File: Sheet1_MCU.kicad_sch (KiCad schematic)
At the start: 16 parts, among them U1 nRF52840-QIAA, Y1 32MHz, Y2 32.77kHz

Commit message: Fix: Applied footprint corrections and added missing libraries to tables
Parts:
- ANT1: footprint Capacitor_SMD:C_0402_1005Metric -> RF_Antenna:Johanson_2450AT18x100
- U1: footprint (none) -> Package_DFN_QFN:Nordic_AQFN-73-1EP_7x7mm_P0.5mm
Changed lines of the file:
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@@
 			)
 		)
-		(property "Footprint" "Capacitor_SMD:C_0402_1005Metric"
+		(property "Footprint" "RF_Antenna:Johanson_2450AT18x100"
 			(at 185 250 0)
 			(effects
@@
 			)
 		)
-		(property "Footprint" ""
+		(property "Footprint" "Package_DFN_QFN:Nordic_AQFN-73-1EP_7x7mm_P0.5mm"
 			(at 200 150 0)
 			(effects

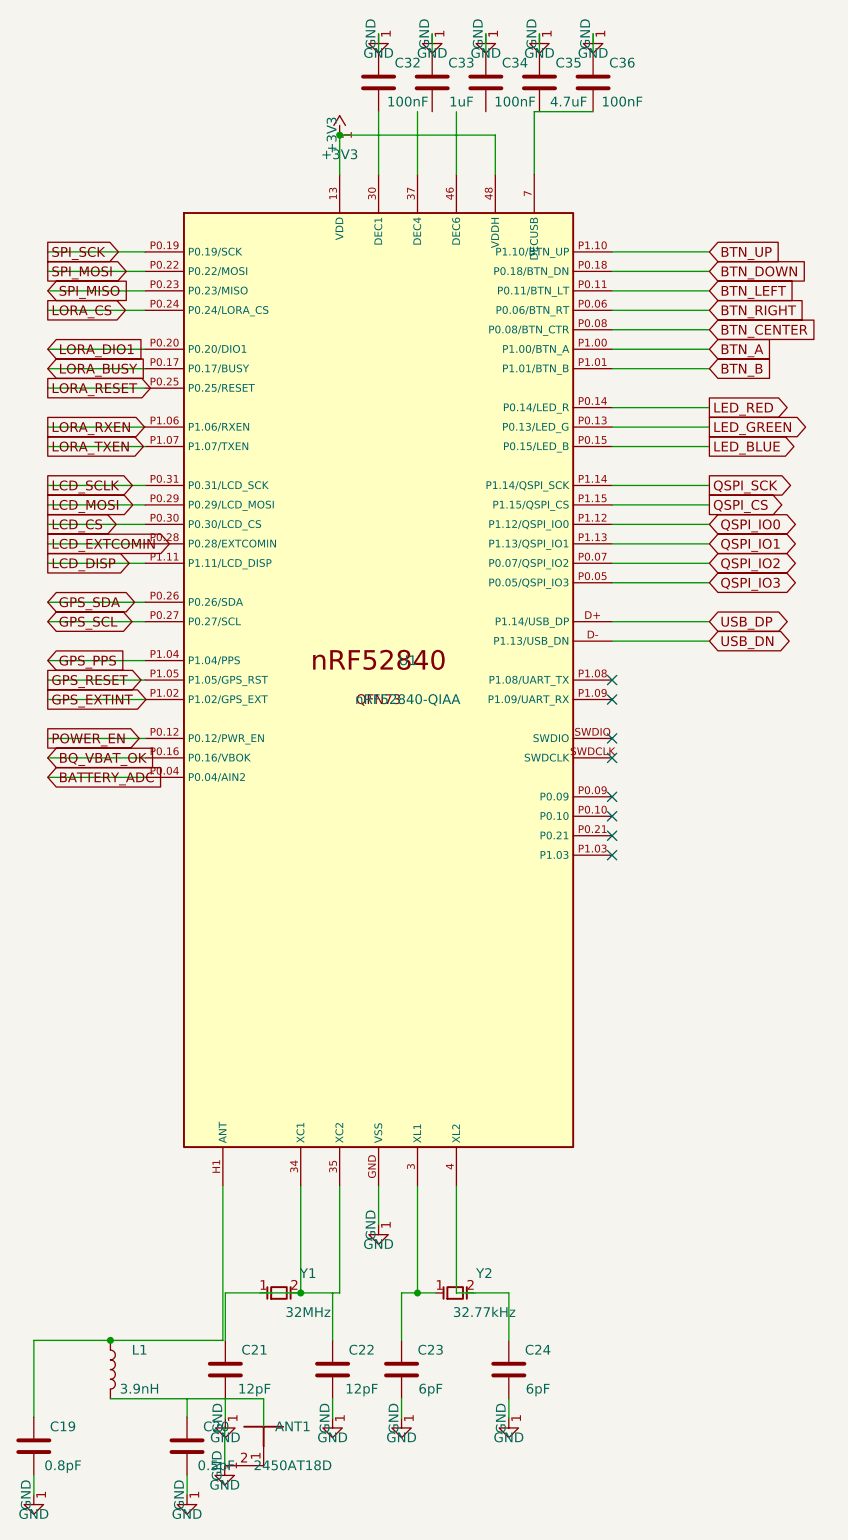
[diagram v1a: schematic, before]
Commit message: Fix: Comprehensive error resolution (nRF52840 pin remapping, footprint rebuilding)
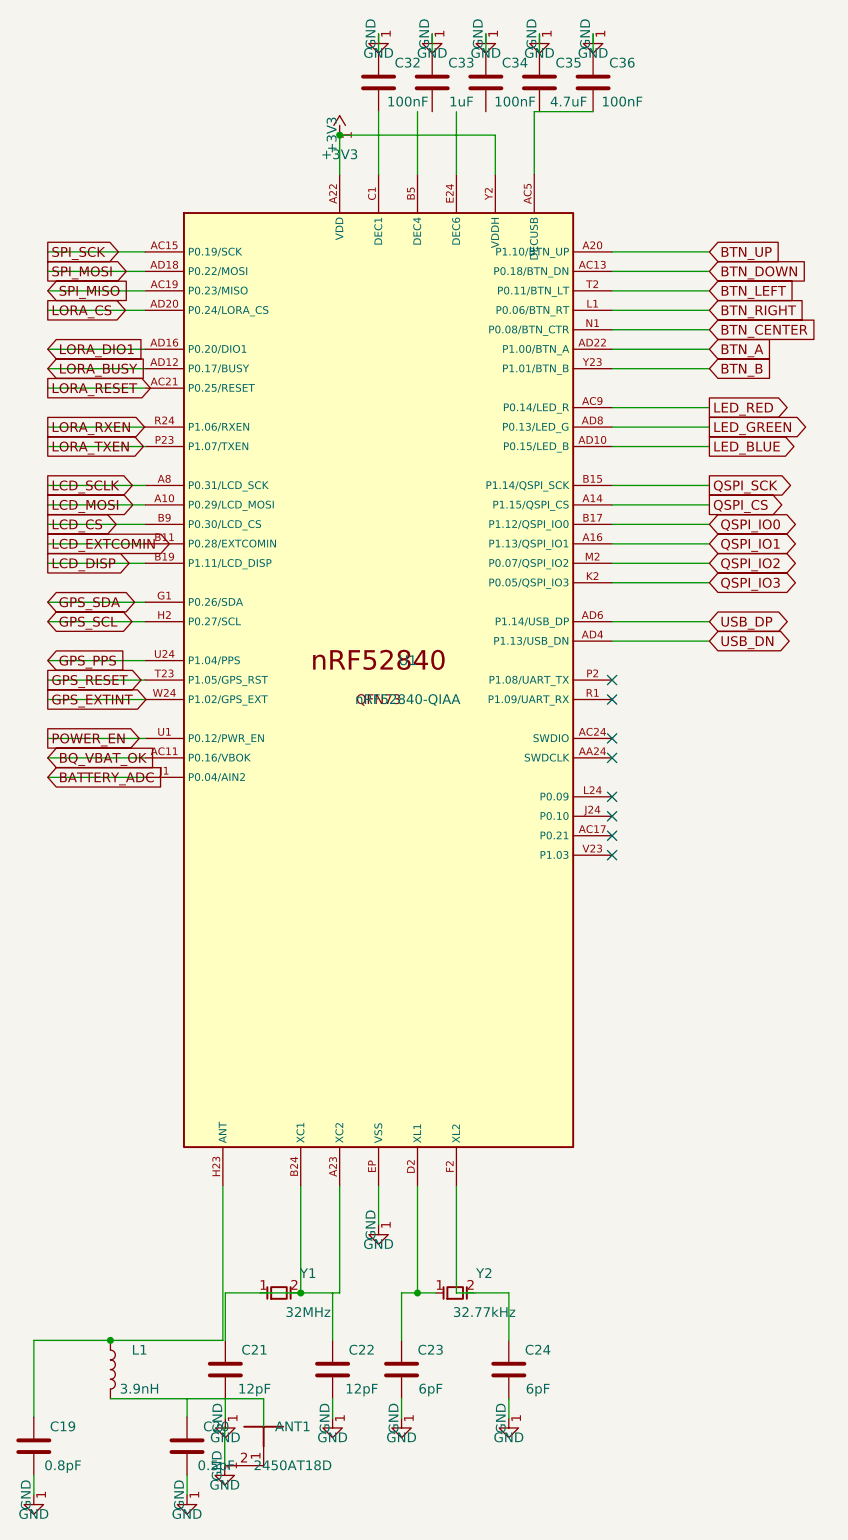
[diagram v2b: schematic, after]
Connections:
- net +3V3: now also U1.A22 (VDD), U1.Y2 (VDDH); no longer U1.13 (VDD), U1.48 (VDDH)
- net BATTERY_ADC: now also U1.J1 (P0.04/AIN2); no longer U1.P0.04 (P0.04/AIN2)
- net BQ_VBAT_OK: now also U1.AC11 (P0.16/VBOK); no longer U1.P0.16 (P0.16/VBOK)
- net BTN_A: now also U1.AD22 (P1.00/BTN_A); no longer U1.P1.00 (P1.00/BTN_A)
- net BTN_B: now also U1.Y23 (P1.01/BTN_B); no longer U1.P1.01 (P1.01/BTN_B)
- net BTN_CENTER: now also U1.N1 (P0.08/BTN_CTR); no longer U1.P0.08 (P0.08/BTN_CTR)
- net BTN_DOWN: now also U1.AC13 (P0.18/BTN_DN); no longer U1.P0.18 (P0.18/BTN_DN)
- net BTN_LEFT: now also U1.T2 (P0.11/BTN_LT); no longer U1.P0.11 (P0.11/BTN_LT)
- net BTN_RIGHT: now also U1.L1 (P0.06/BTN_RT); no longer U1.P0.06 (P0.06/BTN_RT)
- net BTN_UP: now also U1.A20 (P1.10/BTN_UP); no longer U1.P1.10 (P1.10/BTN_UP)
- net GND: now also U1.EP (VSS); no longer U1.GND (VSS)
- net GPS_EXTINT: now also U1.W24 (P1.02/GPS_EXT); no longer U1.P1.02 (P1.02/GPS_EXT)
- net GPS_PPS: now also U1.U24 (P1.04/PPS); no longer U1.P1.04 (P1.04/PPS)
- net GPS_RESET: now also U1.T23 (P1.05/GPS_RST); no longer U1.P1.05 (P1.05/GPS_RST)
- net GPS_SCL: now also U1.H2 (P0.27/SCL); no longer U1.P0.27 (P0.27/SCL)
- net GPS_SDA: now also U1.G1 (P0.26/SDA); no longer U1.P0.26 (P0.26/SDA)
- net LCD_CS: now also U1.B9 (P0.30/LCD_CS); no longer U1.P0.30 (P0.30/LCD_CS)
- net LCD_DISP: now also U1.B19 (P1.11/LCD_DISP); no longer U1.P1.11 (P1.11/LCD_DISP)
- net LCD_EXTCOMIN: now also U1.B11 (P0.28/EXTCOMIN); no longer U1.P0.28 (P0.28/EXTCOMIN)
- net LCD_MOSI: now also U1.A10 (P0.29/LCD_MOSI); no longer U1.P0.29 (P0.29/LCD_MOSI)
- net LCD_SCLK: now also U1.A8 (P0.31/LCD_SCK); no longer U1.P0.31 (P0.31/LCD_SCK)
- net LED_BLUE: now also U1.AD10 (P0.15/LED_B); no longer U1.P0.15 (P0.15/LED_B)
- net LED_GREEN: now also U1.AD8 (P0.13/LED_G); no longer U1.P0.13 (P0.13/LED_G)
- net LED_RED: now also U1.AC9 (P0.14/LED_R); no longer U1.P0.14 (P0.14/LED_R)
- net LORA_BUSY: now also U1.AD12 (P0.17/BUSY); no longer U1.P0.17 (P0.17/BUSY)
- net LORA_CS: now also U1.AD20 (P0.24/LORA_CS); no longer U1.P0.24 (P0.24/LORA_CS)
- net LORA_DIO1: now also U1.AD16 (P0.20/DIO1); no longer U1.P0.20 (P0.20/DIO1)
- net LORA_RESET: now also U1.AC21 (P0.25/RESET); no longer U1.P0.25 (P0.25/RESET)
- net LORA_RXEN: now also U1.R24 (P1.06/RXEN); no longer U1.P1.06 (P1.06/RXEN)
- net LORA_TXEN: now also U1.P23 (P1.07/TXEN); no longer U1.P1.07 (P1.07/TXEN)
- net POWER_EN: now also U1.U1 (P0.12/PWR_EN); no longer U1.P0.12 (P0.12/PWR_EN)
- net QSPI_CS: now also U1.A14 (P1.15/QSPI_CS); no longer U1.P1.15 (P1.15/QSPI_CS)
- net QSPI_IO0: now also U1.B17 (P1.12/QSPI_IO0); no longer U1.P1.12 (P1.12/QSPI_IO0)
- net QSPI_IO1: now also U1.A16 (P1.13/QSPI_IO1); no longer U1.P1.13 (P1.13/QSPI_IO1)
- net QSPI_IO2: now also U1.M2 (P0.07/QSPI_IO2); no longer U1.P0.07 (P0.07/QSPI_IO2)
- net QSPI_IO3: now also U1.K2 (P0.05/QSPI_IO3); no longer U1.P0.05 (P0.05/QSPI_IO3)
- net QSPI_SCK: now also U1.B15 (P1.14/QSPI_SCK); no longer U1.P1.14 (P1.14/QSPI_SCK)
- net SPI_MISO: now also U1.AC19 (P0.23/MISO); no longer U1.P0.23 (P0.23/MISO)
- net SPI_MOSI: now also U1.AD18 (P0.22/MOSI); no longer U1.P0.22 (P0.22/MOSI)
- net SPI_SCK: now also U1.AC15 (P0.19/SCK); no longer U1.P0.19 (P0.19/SCK)
- net USB_DN: now also U1.AD4 (P1.13/USB_DN); no longer U1.D- (P1.13/USB_DN)
- net USB_DP: now also U1.AD6 (P1.14/USB_DP); no longer U1.D+ (P1.14/USB_DP)
- net at C19.1, L1.1: now also U1.H23 (ANT); no longer U1.H1 (ANT)
- net at C36.2: now also U1.AC5 (DECUSB); no longer U1.7 (DECUSB)
- net at C32.2: now also U1.C1 (DEC1); no longer U1.30 (DEC1)
- net at C23.1, Y2.1: now also U1.D2 (XL1); no longer U1.3 (XL1)
- net at C24.1: now also U1.F2 (XL2); no longer U1.4 (XL2)
- new net: C21.1, U1.A23 (XC2), U1.B24 (XC1)
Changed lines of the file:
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@@
 			)
 		)
-		(pin "P0.22"
+		(pin "AD18"
 		)
-		(pin "P0.24"
+		(pin "AD20"
 		)
-		(pin "P0.17"
+		(pin "AD12"
 		)
-		(pin "P1.06"
+		(pin "R24"
 		)
-		(pin "P0.31"
+		(pin "A8"
 		)
-		(pin "P0.19"
+		(pin "AC15"
 		)
-		(pin "P0.23"
+		(pin "AC19"
 		)
-		(pin "P0.20"
+		(pin "AD16"
 		)
-		(pin "P0.25"
+		(pin "AC21"
 		)
-		(pin "P1.07"
+		(pin "P23"
 		)
-		(pin "P1.11"
+		(pin "B19"
 		)
-		(pin "P0.27"
+		(pin "H2"
 		)
-		(pin "P1.04"
+		(pin "U24"
 		)
-		(pin "P1.02"
+		(pin "W24"
 		)
-		(pin "30"
+		(pin "C1"
 		)
-		(pin "P1.05"
+		(pin "T23"
 		)
-		(pin "P0.12"
+		(pin "U1"
 		)
-		(pin "37"
+		(pin "B5"
 		)
-		(pin "P0.26"
+		(pin "G1"
 		)
-		(pin "H1"
+		(pin "H23"
 		)
-		(pin "P0.28"
+		(pin "B11"
 		)
-		(pin "34"
+		(pin "B24"
 		)
-		(pin "P0.04"
+		(pin "J1"
 		)
-		(pin "P0.29"
+		(pin "A10"
 		)
-		(pin "35"
+		(pin "A23"
 		)
-		(pin "GND"
+		(pin "EP"
 		)
-		(pin "P0.16"
+		(pin "AC11"
 		)
-		(pin "13"
+		(pin "A22"
 		)
-		(pin "P0.30"
+		(pin "B9"
 		)
-		(pin "D+"
+		(pin "AD6"
 		)
-		(pin "P1.08"
+		(pin "P2"
 		)
-		(pin "SWDIO"
+		(pin "AC24"
 		)
-		(pin "48"
+		(pin "Y2"
 		)
-		(pin "7"
+		(pin "AC5"
 		)
-		(pin "3"
+		(pin "D2"
 		)
-		(pin "P1.15"
+		(pin "A14"
 		)
-		(pin "4"
+		(pin "F2"
 		)
-		(pin "P0.11"
+		(pin "T2"
 		)
-		(pin "P1.00"
+		(pin "AD22"
 		)
-		(pin "P0.06"
+		(pin "L1"
 		)
-		(pin "46"
+		(pin "E24"
 		)
-		(pin "P0.08"
+		(pin "N1"
 		)
-		(pin "P1.10"
+		(pin "A20"
 		)
-		(pin "P1.01"
+		(pin "Y23"
 		)
-		(pin "P0.14"
+		(pin "AC9"
 		)
-		(pin "P0.13"
+		(pin "AD8"
 		)
-		(pin "P0.15"
+		(pin "AD10"
 		)
-		(pin "P1.14"
+		(pin "B15"
 		)
-		(pin "P1.12"
+		(pin "B17"
 		)
-		(pin "P1.13"
+		(pin "A16"
 		)
-		(pin "P0.18"
+		(pin "AC13"
 		)
-		(pin "P0.07"
+		(pin "M2"
 		)
-		(pin "P0.05"
+		(pin "K2"
 		)
-		(pin "D-"
+		(pin "AD4"
 		)
-		(pin "P1.09"
+		(pin "R1"
 		)
-		(pin "SWDCLK"
+		(pin "AA24"
 		)
-		(pin "P0.09"
+		(pin "L24"
 		)
-		(pin "P0.10"
+		(pin "J24"
 		)
-		(pin "P0.21"
+		(pin "AC17"
 		)
-		(pin "P1.03"
+		(pin "V23"
 		)
 		(instances
